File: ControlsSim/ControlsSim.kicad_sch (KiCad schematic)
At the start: 25 parts, among them J2 Accelerator Pot, J3 Brake Button, J5 Motor Contactors, J6 Array Contactors, J7 Rotary Switch, SW2 SW_Rotary2x6

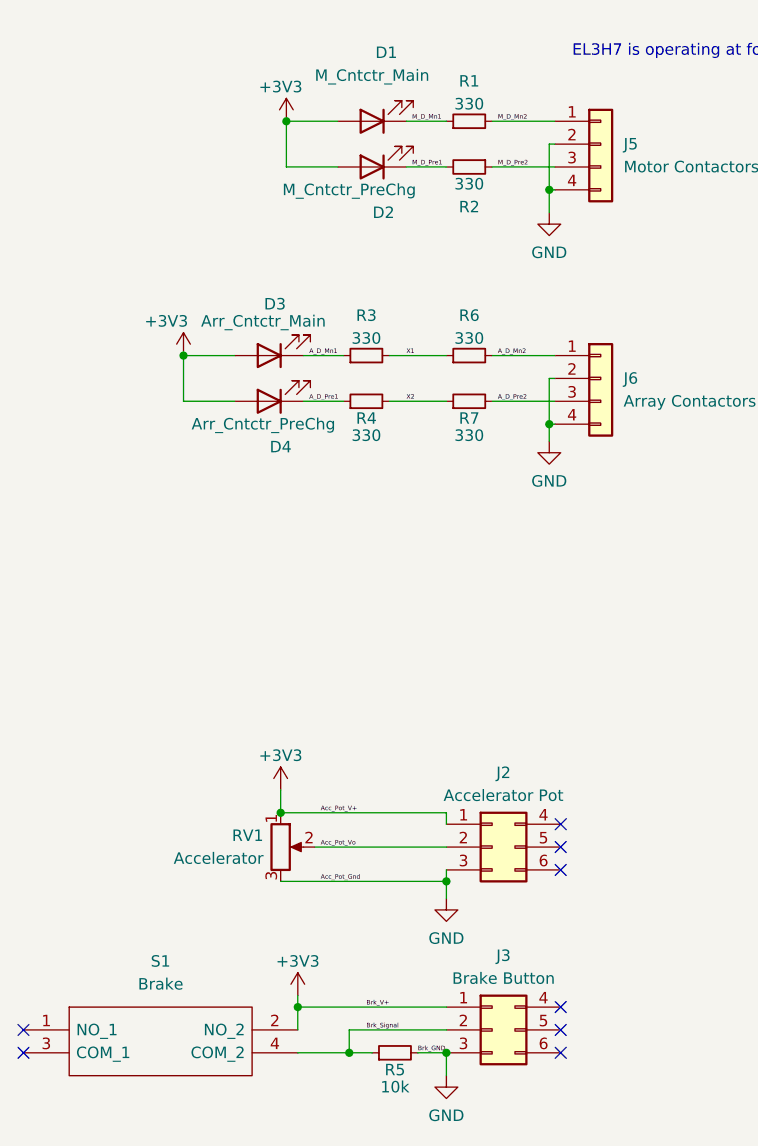
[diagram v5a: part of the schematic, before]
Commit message: Changed LED colors to use all four colors, one for each contactor
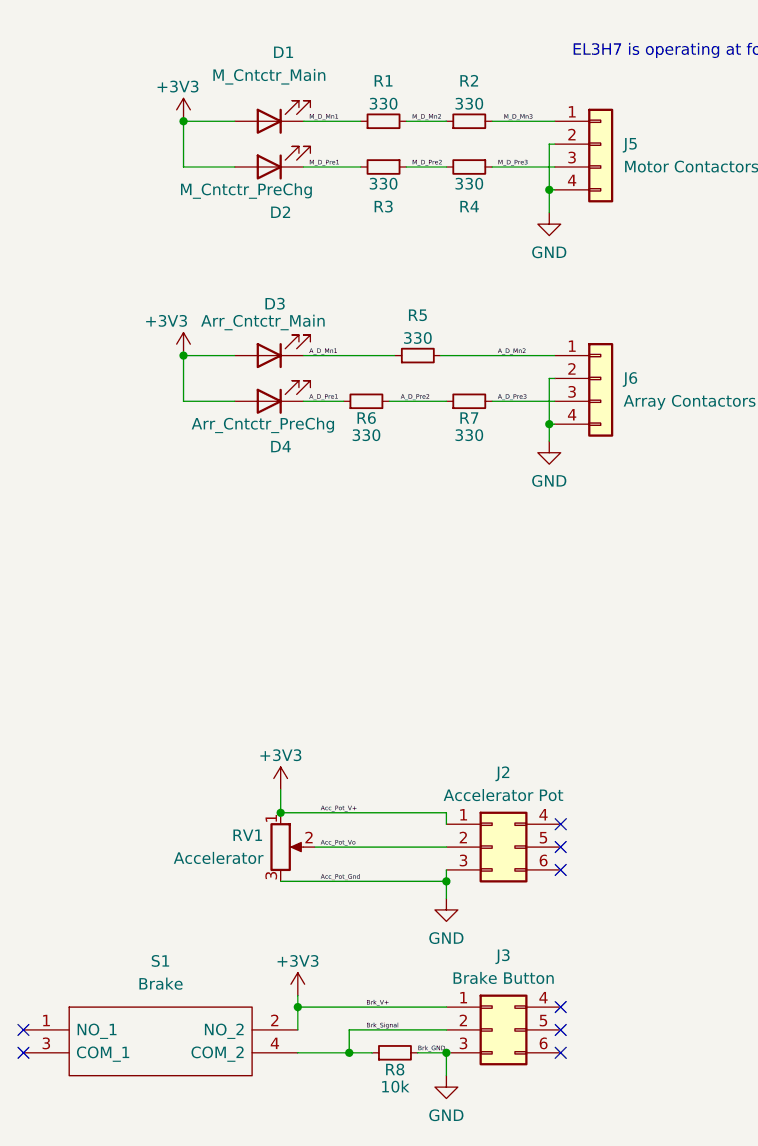
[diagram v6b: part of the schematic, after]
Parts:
- added R1: 330, Resistor_SMD:R_0805_2012Metric, symbol Device:R_Small
- D1: Color (none) -> Yellow; MFG PN APTD2012LVBC/D -> APTD2012LSYCK
- D2: Color (none) -> Red; MFG PN APTD2012LVBC/D -> APTD2012LSURCK
- D3: Color (none) -> Blue; MFG PN (none) -> APTD2012LVBC/D
- D4: Color (none) -> Green; MFG PN (none) -> APTD2012LCGCK
- renumbered R1 to R2, R2 to R4, R6 to R5, R4 to R6, R5 to R8
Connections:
- net X2 is gone; now on net A_D_Pre2: R6.2, R7.1
- net A_D_Mn1: now also R5.1; no longer R3.1
- net A_D_Pre2: no longer J6.3 (Pin_3), R7.2
- net M_D_Mn1: now also R1.1; no longer R2.1
- net M_D_Mn2: now also R2.1, R1.2; no longer J5.1 (Pin_1), R2.2
- net M_D_Pre1: now also R3.2; no longer R4.2
- net M_D_Pre2: now also R3.1, R4.2; no longer J5.3 (Pin_3), R4.1
- removed net X1: R3.2, R5.1
- new net A_D_Pre3: J6.3 (Pin_3), R7.2
- new net M_D_Mn3: J5.1 (Pin_1), R2.2
- new net M_D_Pre3: J5.3 (Pin_3), R4.1
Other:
- moved on the sheet: D1, D2, R5
